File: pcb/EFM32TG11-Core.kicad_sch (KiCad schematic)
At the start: 53 parts, among them J1 PWR_IN, J2 EXT_PWR, J3 EXT_UART, J4 EXT_I2C, J5 BOOT, J6 Conn_ARM_JTAG_SWD_10, J7 GPIO_HI, J8 GPIO_LO, Q1 Si2301CDS, SW1 SW_Push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

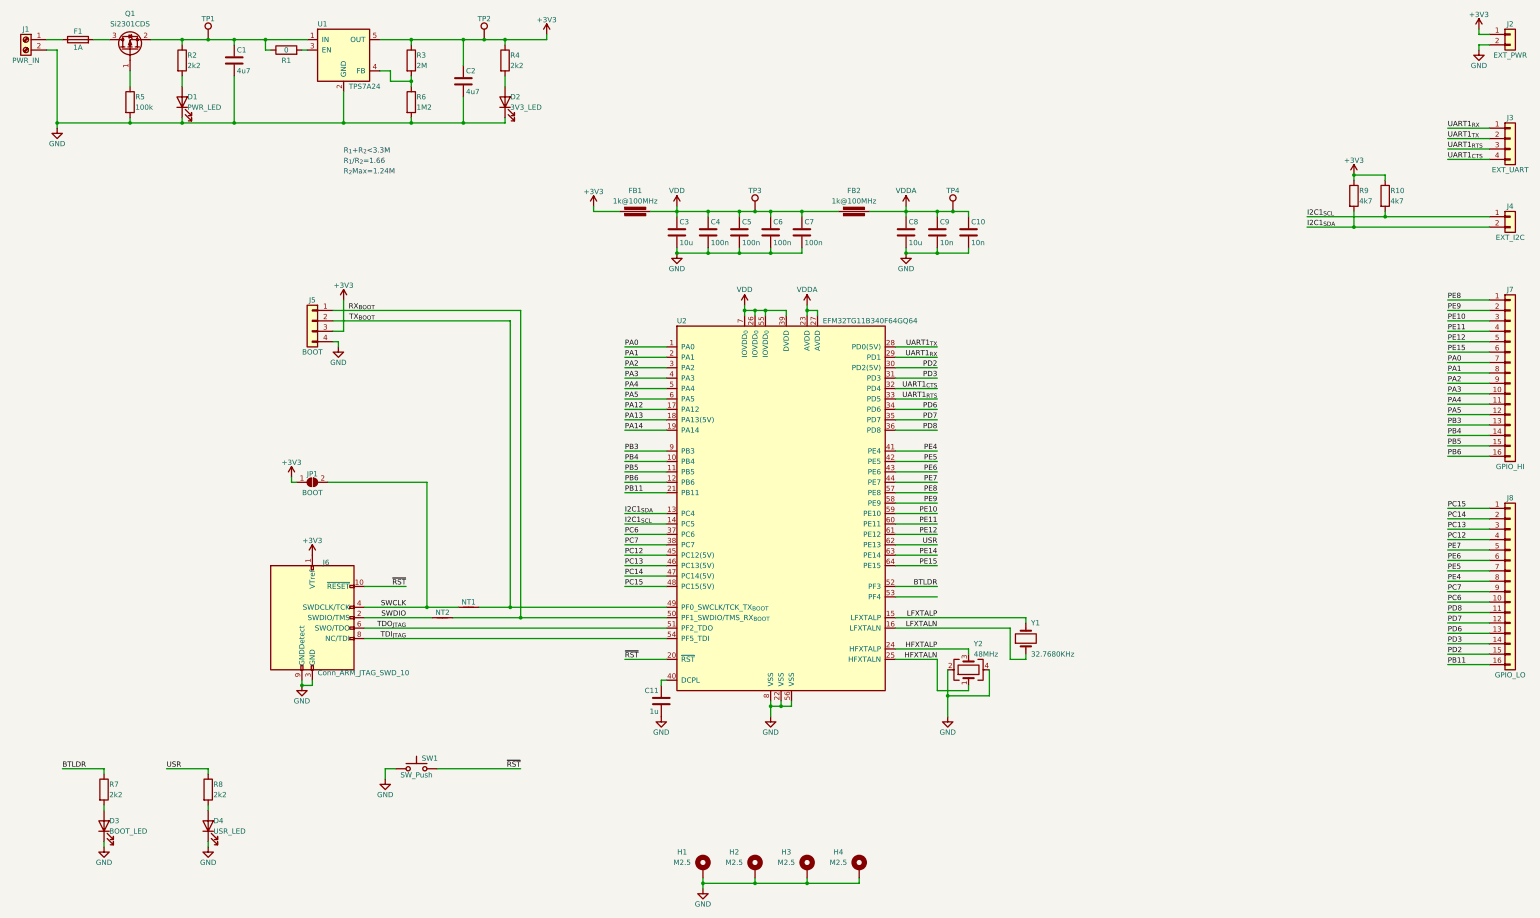
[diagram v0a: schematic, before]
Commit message: Reorganization of schematic to heirarchical sheets
Took single sheet schematic and reorganized to 3 heirarchical sheets.
This allowed for the schematic to be printable on 8.5"x11" sheets of
paper without losing clarity of the schematic. All reference
designators were maintained.

Buses and interconnects between pages still need to be added to the
schematic to finish transition.

[Issue: X]
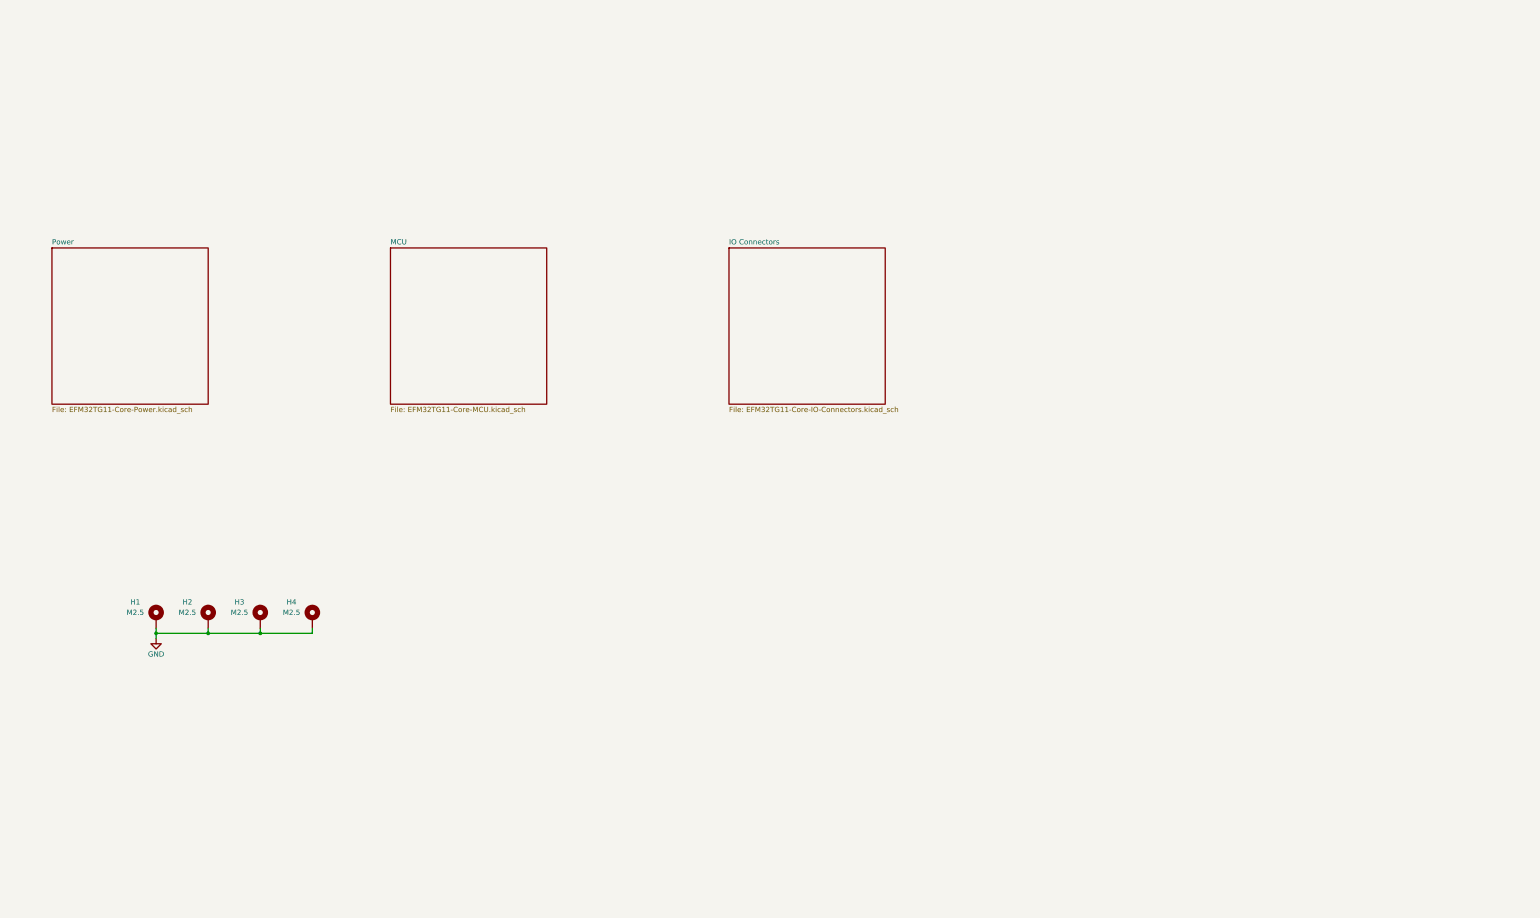
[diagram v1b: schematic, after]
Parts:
- removed C1, C2: 4u7, Capacitor_SMD:C_0805_2012Metric, symbol Device:C
- removed C10, C9: 10n, Capacitor_SMD:C_0603_1608Metric, symbol Device:C
- removed C11: 1u, Capacitor_SMD:C_0603_1608Metric, symbol Device:C
- removed C3, C8: 10u, Capacitor_SMD:C_1206_3216Metric, symbol Device:C
- removed C4, C5, C6, C7: 100n, Capacitor_SMD:C_0603_1608Metric, symbol Device:C
- removed D1: PWR_LED, Diode_SMD:D_0603_1608Metric_Pad1.05x0.95mm_HandSolder, symbol Device:LED
- removed D2: 3V3_LED, Diode_SMD:D_0603_1608Metric_Pad1.05x0.95mm_HandSolder, symbol Device:LED
- removed D3: BOOT_LED, Diode_SMD:D_0603_1608Metric_Pad1.05x0.95mm_HandSolder, symbol Device:LED
- removed D4: USR_LED, Diode_SMD:D_0603_1608Metric_Pad1.05x0.95mm_HandSolder, symbol Device:LED
- removed F1: 1A, Fuse:Fuse_0603_1608Metric, symbol Device:Fuse
- removed FB1, FB2: 1k@100MHz, Inductor_SMD:L_0603_1608Metric, symbol Device_AKL:Ferrite_Bead
- removed J1: PWR_IN, TerminalBlock_Phoenix:TerminalBlock_Phoenix_PT-1,5-2-3.5-H_1x02_P3.50mm_Horizontal, symbol Connector:Screw_Terminal_01x02
- removed J2: EXT_PWR, Connector_PinHeader_2.54mm:PinHeader_1x02_P2.54mm_Horizontal, symbol Connector_Generic:Conn_01x02
- removed J3: EXT_UART, Connector_PinHeader_2.54mm:PinHeader_1x04_P2.54mm_Horizontal, symbol Connector_Generic:Conn_01x04
- removed J4: EXT_I2C, Connector_PinHeader_2.54mm:PinHeader_1x02_P2.54mm_Horizontal, symbol Connector_Generic:Conn_01x02
- removed J5: BOOT, Connector_PinHeader_2.54mm:PinHeader_1x04_P2.54mm_Horizontal, symbol Connector_Generic:Conn_01x04
- removed J6: Conn_ARM_JTAG_SWD_10, Connector_PinHeader_1.27mm:PinHeader_2x05_P1.27mm_Vertical, symbol Connector:Conn_ARM_JTAG_SWD_10
- removed J7: GPIO_HI, Connector_PinSocket_2.54mm:PinSocket_1x16_P2.54mm_Vertical, symbol Connector_Generic:Conn_01x16
- removed J8: GPIO_LO, Connector_PinSocket_2.54mm:PinSocket_1x16_P2.54mm_Vertical, symbol Connector_Generic:Conn_01x16
- removed JP1: BOOT, Jumper:SolderJumper-2_P1.3mm_Open_RoundedPad1.0x1.5mm, symbol Jumper:SolderJumper_2_Open
- removed NT1, NT2: NetTie_2, NetTie:NetTie-2_THT_Pad0.3mm, symbol Device:NetTie_2
- removed Q1: Si2301CDS, Package_TO_SOT_SMD:SOT-23, symbol Device:Q_PMOS_GSD
- removed R1: 0, Resistor_SMD:R_0603_1608Metric, symbol Device:R
- removed R10, R9: 4k7, Resistor_SMD:R_0603_1608Metric, symbol Device:R
- removed R2, R4, R7, R8: 2k2, Resistor_SMD:R_0603_1608Metric, symbol Device:R
- removed R3: 2M, Resistor_SMD:R_0603_1608Metric, symbol Device:R
- removed R5: 100k, Resistor_SMD:R_0603_1608Metric, symbol Device:R
- removed R6: 1M2, Resistor_SMD:R_0603_1608Metric, symbol Device:R
- removed SW1: SW_Push, Button_Switch_SMD:SW_SPST_CK_RS282G05A3, symbol Switch:SW_Push
- removed TP1, TP2, TP3, TP4: TestPoint, TestPoint:TestPoint_Pad_D1.0mm, symbol Connector:TestPoint
- removed U1: TPS7A24, Package_TO_SOT_SMD:SOT-23-5, symbol Regulator_Linear_NS:TPS7A24
- removed U2: EFM32TG11B340F64GQ64, Package_QFP:TQFP-64_10x10mm_P0.5mm, symbol MCU_SiLabs_EFM32TG11:EFM32TG11B340F64GQ64
- removed Y1: 32.7680KHz, Crystal:Crystal_SMD_MicroCrystal_CC7V-T1A-2Pin_3.2x1.5mm, symbol Device:Crystal
- removed Y2: 48MHz, Crystal:Crystal_SMD_2016-4Pin_2.0x1.6mm, symbol Device:Crystal_GND24
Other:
- added sheet IO Connectors (EFM32TG11-Core-IO-Connectors.kicad_sch)
- added sheet MCU (EFM32TG11-Core-MCU.kicad_sch)
- added sheet Power (EFM32TG11-Core-Power.kicad_sch)
- note removed: "R_{1}+R_{2}<3.3M"
- note removed: "R_{1}/R_{2}=1.66"
- note removed: "R_{2}Max=1.24M"
- company: NS-Industries -> Project: EFM32TG11-Core
- title: (none) -> EFM32TG11-Core
- moved on the sheet: H1, H2, H3, H4

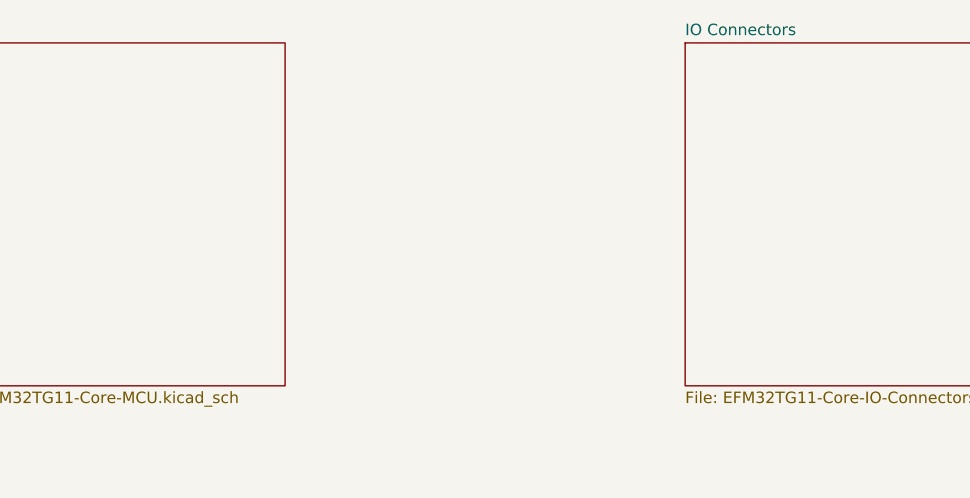
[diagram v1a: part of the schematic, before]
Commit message: Fix Nets for Hierarchical Sheets
Defined busses to pass nets to and from MCU sheet and IO connector
sheet.
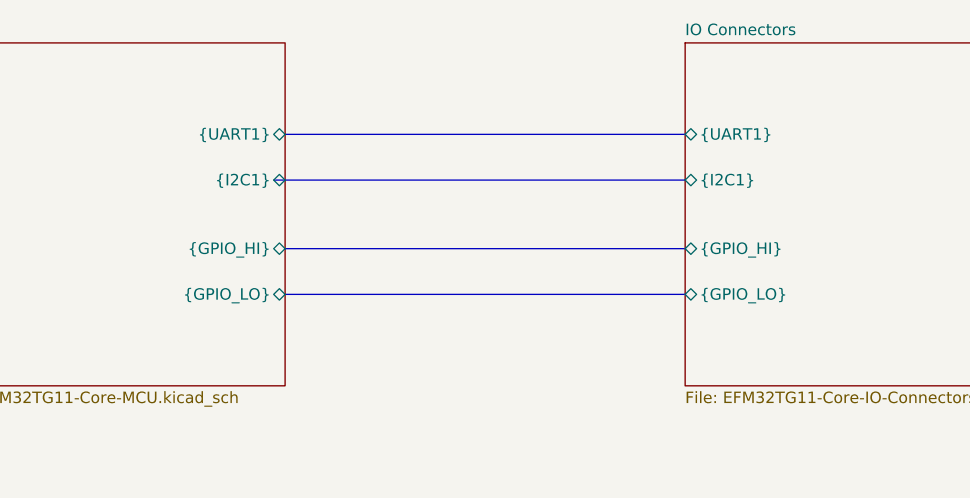
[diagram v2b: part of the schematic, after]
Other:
- sheet IO Connectors ports: added {GPIO_HI}, {GPIO_LO}, {I2C1}, {UART1}; removed none
- sheet MCU ports: added {GPIO_HI}, {GPIO_LO}, {I2C1}, {UART1}; removed none
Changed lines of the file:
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@@
   (junction (at 88.9 170.18) (diameter 0) (color 0 0 0 0)
+  )
+  (bus (pts (xy 158.75 86.36) (xy 203.2 86.36))
+    (stroke (width 0) (type default) (color 0 0 0 0))
   )
   (wire (pts (xy 76.2 170.18) (xy 63.5 170.18))
@@
     (stroke (width 0) (type default) (color 0 0 0 0))
   )
+  (bus (pts (xy 158.75 99.06) (xy 203.2 99.06))
+    (stroke (width 0) (type default) (color 0 0 0 0))
+  )
+  (bus (pts (xy 157.48 91.44) (xy 203.2 91.44))
+    (stroke (width 0) (type default) (color 0 0 0 0))
+  )
   (wire (pts (xy 101.6 168.91) (xy 101.6 170.18))
+    (stroke (width 0) (type default) (color 0 0 0 0))
+  )
+  (bus (pts (xy 158.75 104.14) (xy 203.2 104.14))
     (stroke (width 0) (type default) (color 0 0 0 0))
   )
@@
       (effects (font (size 1.27 1.27)) (justify left top))
     )
+    (pin "{I2C1}" bidirectional (at 158.75 91.44 0)
+      (effects (font (size 1.27 1.27)) (justify right))
+    )
+    (pin "{UART1}" bidirectional (at 158.75 86.36 0)
+      (effects (font (size 1.27 1.27)) (justify right))
+    )
+    (pin "{GPIO_HI}" bidirectional (at 158.75 99.06 0)
+      (effects (font (size 1.27 1.27)) (justify right))
+    )
+    (pin "{GPIO_LO}" bidirectional (at 158.75 104.14 0)
+      (effects (font (size 1.27 1.27)) (justify right))
+    )
   )
   (sheet (at 203.2 76.2) (size 38.1 38.1) (fields_autoplaced)
@@
       (effects (font (size 1.27 1.27)) (justify left top))
     )
+    (pin "{UART1}" bidirectional (at 203.2 86.36 180)
+      (effects (font (size 1.27 1.27)) (justify left))
+    )
+    (pin "{I2C1}" bidirectional (at 203.2 91.44 180)
+      (effects (font (size 1.27 1.27)) (justify left))
+    )
+    (pin "{GPIO_LO}" bidirectional (at 203.2 104.14 180)
+      (effects (font (size 1.27 1.27)) (justify left))
+    )
+    (pin "{GPIO_HI}" bidirectional (at 203.2 99.06 180)
+      (effects (font (size 1.27 1.27)) (justify left))
+    )
   )
